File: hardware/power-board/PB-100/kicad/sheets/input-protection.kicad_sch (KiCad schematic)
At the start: 6 parts, among them J1 INPUT_CONNECTOR_CLASS_PRELIM, Q1 INPUT_NMOS_TOLL_PRELIM, U1 LM74700QDBVRQ1_PRELIM, U2 INA228_Q1_PRELIM

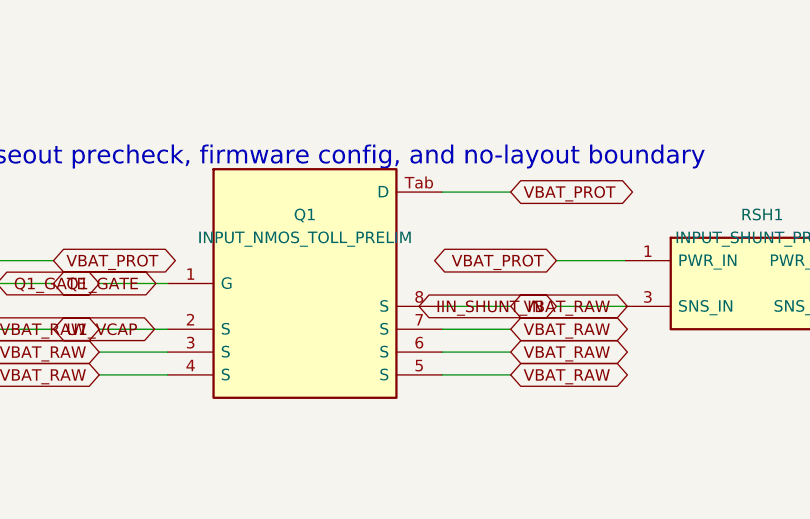
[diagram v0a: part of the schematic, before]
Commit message: feat(hardware): accept CAN1 and 80V freeze decisions
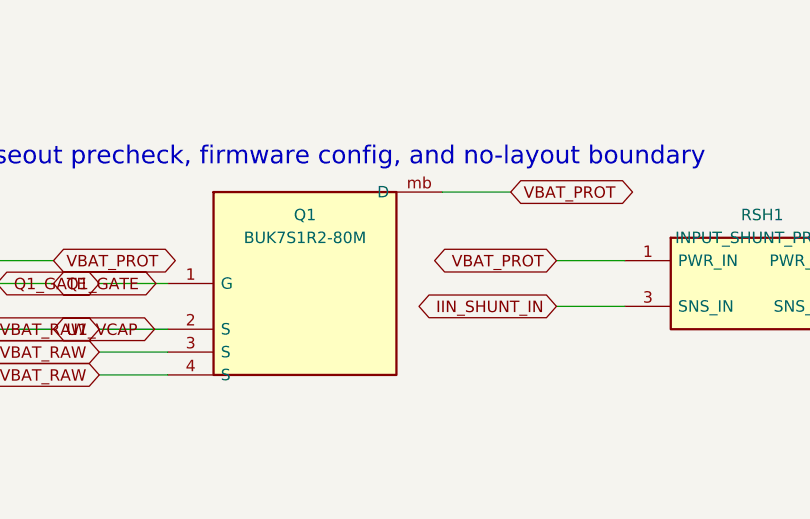
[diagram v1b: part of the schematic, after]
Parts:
- Q1: value INPUT_NMOS_TOLL_PRELIM -> BUK7S1R2-80M; footprint (none) -> PB100:LFPAK88_SOT1235_Nexperia; symbol PB100:PB100_INPUT_NMOS_TOLL_PRELIM -> PB100:PB100_POWER_NMOS_ESCAPE_PRELIM
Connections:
- net VBAT_PROT: now also Q1.mb (D); no longer Q1.Tab (D)
- net VBAT_RAW: no longer Q1.5 (S), Q1.6 (S), Q1.7 (S), Q1.8 (S)
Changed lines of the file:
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@@
   (global_label "VBAT_RAW" (shape bidirectional) (at 129.54 55.88 0) (fields_autoplaced) (effects (font (size 1.27 1.27)) (justify right)) (property "Intersheetrefs" "${INTERSHEET_REFS}" (at 129.54 55.88 0) (effects (font (size 1.27 1.27)) hide)))
   (symbol
-    (lib_id "PB100:PB100_INPUT_NMOS_TOLL_PRELIM")
+    (lib_id "PB100:PB100_POWER_NMOS_ESCAPE_PRELIM")
     (at 203.20 60.96 0)
     (unit 1)
@@
     (dnp no)
     (property "Reference" "Q1" (at 203.20 53.34 0) (effects (font (size 1.27 1.27))))
-    (property "Value" "INPUT_NMOS_TOLL_PRELIM" (at 203.20 55.88 0) (effects (font (size 1.27 1.27))))
-    (property "Footprint" "" (at 203.20 68.58 0) (effects (font (size 1.27 1.27)) hide))
-    (property "Datasheet" "../PB-100-schematic-capture-plan.md" (at 203.20 71.12 0) (effects (font (size 1.27 1.27)) hide))
+    (property "Value" "BUK7S1R2-80M" (at 203.20 55.88 0) (effects (font (size 1.27 1.27))))
+    (property "Footprint" "PB100:LFPAK88_SOT1235_Nexperia" (at 203.20 68.58 0) (effects (font (size 1.27 1.27)) hide))
+    (property "Datasheet" "https://assets.nexperia.com/documents/data-sheet/BUK7S1R2-80M.pdf" (at 203.20 71.12 0) (effects (font (size 1.27 1.27)) hide))
     (pin "1")
     (pin "2")
     (pin "3")
     (pin "4")
-    (pin "5")
-    (pin "6")
-    (pin "7")
-    (pin "8")
-    (pin "Tab")
+    (pin "mb")
     (instances
       (project "PB-100"
@@
   (wire (pts (xy 187.96 71.12) (xy 180.34 71.12)) (stroke (width 0) (type default)))
   (global_label "VBAT_RAW" (shape bidirectional) (at 180.34 71.12 0) (fields_autoplaced) (effects (font (size 1.27 1.27)) (justify right)) (property "Intersheetrefs" "${INTERSHEET_REFS}" (at 180.34 71.12 0) (effects (font (size 1.27 1.27)) hide)))
-  (wire (pts (xy 218.44 71.12) (xy 226.06 71.12)) (stroke (width 0) (type default)))
-  (global_label "VBAT_RAW" (shape bidirectional) (at 226.06 71.12 0) (fields_autoplaced) (effects (font (size 1.27 1.27)) (justify left)) (property "Intersheetrefs" "${INTERSHEET_REFS}" (at 226.06 71.12 0) (effects (font (size 1.27 1.27)) hide)))
-  (wire (pts (xy 218.44 68.58) (xy 226.06 68.58)) (stroke (width 0) (type default)))
-  (global_label "VBAT_RAW" (shape bidirectional) (at 226.06 68.58 0) (fields_autoplaced) (effects (font (size 1.27 1.27)) (justify left)) (property "Intersheetrefs" "${INTERSHEET_REFS}" (at 226.06 68.58 0) (effects (font (size 1.27 1.27)) hide)))
-  (wire (pts (xy 218.44 66.04) (xy 226.06 66.04)) (stroke (width 0) (type default)))
-  (global_label "VBAT_RAW" (shape bidirectional) (at 226.06 66.04 0) (fields_autoplaced) (effects (font (size 1.27 1.27)) (justify left)) (property "Intersheetrefs" "${INTERSHEET_REFS}" (at 226.06 66.04 0) (effects (font (size 1.27 1.27)) hide)))
-  (wire (pts (xy 218.44 63.50) (xy 226.06 63.50)) (stroke (width 0) (type default)))
-  (global_label "VBAT_RAW" (shape bidirectional) (at 226.06 63.50 0) (fields_autoplaced) (effects (font (size 1.27 1.27)) (justify left)) (property "Intersheetrefs" "${INTERSHEET_REFS}" (at 226.06 63.50 0) (effects (font (size 1.27 1.27)) hide)))
   (wire (pts (xy 218.44 50.80) (xy 226.06 50.80)) (stroke (width 0) (type default)))
   (global_label "VBAT_PROT" (shape bidirectional) (at 226.06 50.80 0) (fields_autoplaced) (effects (font (size 1.27 1.27)) (justify left)) (property "Intersheetrefs" "${INTERSHEET_REFS}" (at 226.06 50.80 0) (effects (font (size 1.27 1.27)) hide)))

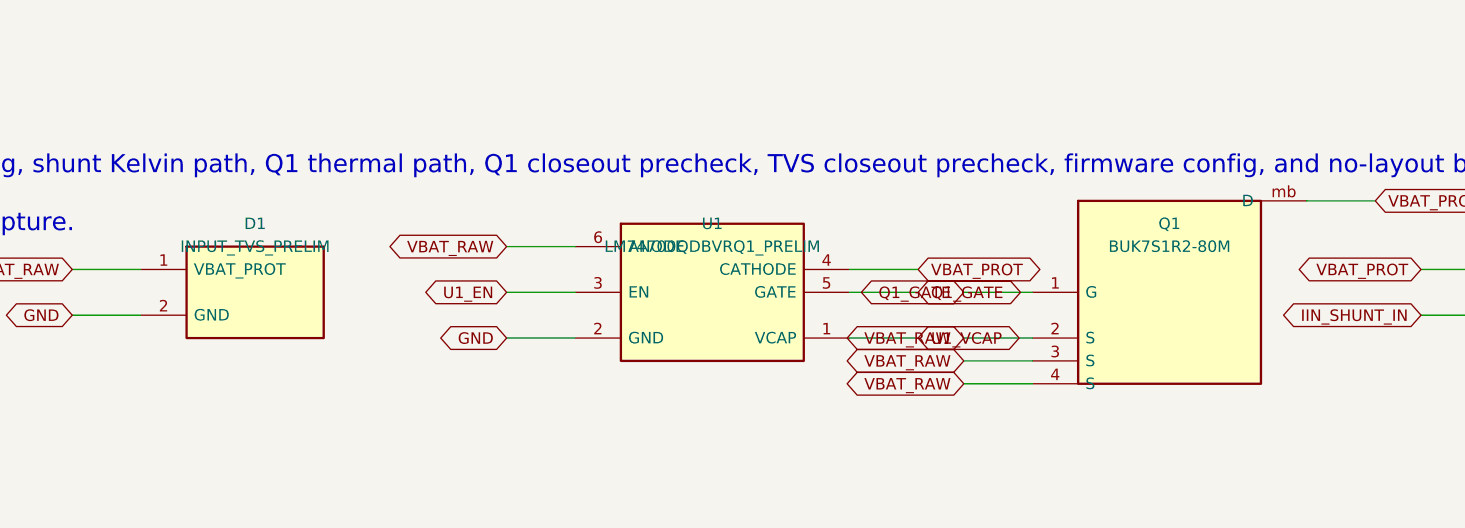
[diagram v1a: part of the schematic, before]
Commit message: feat(pb100): close five pre-layout blockers with generated evidence
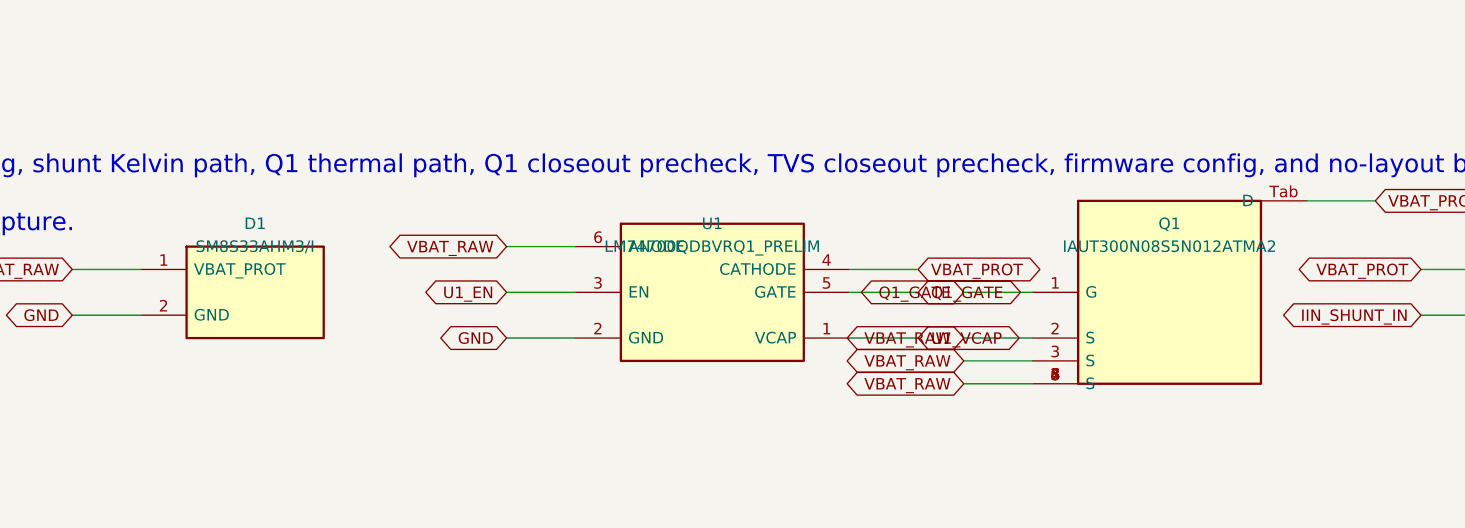
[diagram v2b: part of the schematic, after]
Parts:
- D1: value INPUT_TVS_PRELIM -> SM8S33AHM3/I; footprint (none) -> PB100:DO-218AC_Vishay_SM8S; symbol PB100:PB100_INPUT_TVS_PRELIM -> PB100:PB100_SM8S33AHM3I
- Q1: value BUK7S1R2-80M -> IAUT300N08S5N012ATMA2; footprint PB100:LFPAK88_SOT1235_Nexperia -> PB100:PG-HSOF-8-1_TOLL_Infineon; symbol PB100:PB100_POWER_NMOS_ESCAPE_PRELIM -> PB100:PB100_POWER_NMOS_TOLL_80V
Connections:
- net VBAT_PROT: now also Q1.Tab (D); no longer Q1.mb (D)
- net VBAT_RAW: now also Q1.5 (S), Q1.6 (S), Q1.7 (S), Q1.8 (S)
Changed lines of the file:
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@@
   (global_label "GND_IN" (shape bidirectional) (at 27.94 63.50 0) (fields_autoplaced) (effects (font (size 1.27 1.27)) (justify right)) (property "Intersheetrefs" "${INTERSHEET_REFS}" (at 27.94 63.50 0) (effects (font (size 1.27 1.27)) hide)))
   (symbol
-    (lib_id "PB100:PB100_INPUT_TVS_PRELIM")
+    (lib_id "PB100:PB100_SM8S33AHM3I")
     (at 101.60 60.96 0)
     (unit 1)
@@
     (dnp no)
     (property "Reference" "D1" (at 101.60 53.34 0) (effects (font (size 1.27 1.27))))
-    (property "Value" "INPUT_TVS_PRELIM" (at 101.60 55.88 0) (effects (font (size 1.27 1.27))))
-    (property "Footprint" "" (at 101.60 68.58 0) (effects (font (size 1.27 1.27)) hide))
-    (property "Datasheet" "../PB-100-schematic-capture-plan.md" (at 101.60 71.12 0) (effects (font (size 1.27 1.27)) hide))
+    (property "Value" "SM8S33AHM3/I" (at 101.60 55.88 0) (effects (font (size 1.27 1.27))))
+    (property "Footprint" "PB100:DO-218AC_Vishay_SM8S" (at 101.60 68.58 0) (effects (font (size 1.27 1.27)) hide))
+    (property "Datasheet" "https://www.vishay.com/docs/88392/sm8s.pdf" (at 101.60 71.12 0) (effects (font (size 1.27 1.27)) hide))
     (pin "1")
     (pin "2")
@@
   (global_label "VBAT_RAW" (shape bidirectional) (at 129.54 55.88 0) (fields_autoplaced) (effects (font (size 1.27 1.27)) (justify right)) (property "Intersheetrefs" "${INTERSHEET_REFS}" (at 129.54 55.88 0) (effects (font (size 1.27 1.27)) hide)))
   (symbol
-    (lib_id "PB100:PB100_POWER_NMOS_ESCAPE_PRELIM")
+    (lib_id "PB100:PB100_POWER_NMOS_TOLL_80V")
     (at 203.20 60.96 0)
     (unit 1)
@@
     (dnp no)
     (property "Reference" "Q1" (at 203.20 53.34 0) (effects (font (size 1.27 1.27))))
-    (property "Value" "BUK7S1R2-80M" (at 203.20 55.88 0) (effects (font (size 1.27 1.27))))
-    (property "Footprint" "PB100:LFPAK88_SOT1235_Nexperia" (at 203.20 68.58 0) (effects (font (size 1.27 1.27)) hide))
-    (property "Datasheet" "https://assets.nexperia.com/documents/data-sheet/BUK7S1R2-80M.pdf" (at 203.20 71.12 0) (effects (font (size 1.27 1.27)) hide))
+    (property "Value" "IAUT300N08S5N012ATMA2" (at 203.20 55.88 0) (effects (font (size 1.27 1.27))))
+    (property "Footprint" "PB100:PG-HSOF-8-1_TOLL_Infineon" (at 203.20 68.58 0) (effects (font (size 1.27 1.27)) hide))
+    (property "Datasheet" "https://www.infineon.com/assets/row/public/documents/10/49/infineon-iaut300n08s5n012-datasheet-en.pdf" (at 203.20 71.12 0) (effects (font (size 1.27 1.27)) hide))
     (pin "1")
     (pin "2")
     (pin "3")
     (pin "4")
-    (pin "mb")
+    (pin "5")
+    (pin "6")
+    (pin "7")
+    (pin "8")
+    (pin "Tab")
     (instances
       (project "PB-100"

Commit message: fix(pb100): select active surge cutoff architecture
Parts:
- added CCAP1: 100nF 25V X7R, symbol PB100:PB100_TWO_PIN_COMPONENT
- added CVS1: 100nF 100V X7R, symbol PB100:PB100_TWO_PIN_COMPONENT
- added DZVS1: 56V automotive Zener, symbol PB100:PB100_TWO_PIN_COMPONENT
- added Q2: IAUTN15S6N025ATMA1, PB100:PG-HSOF-8-1_TOLL_Infineon, symbol PB100:PB100_POWER_NMOS_TOLL_150V
- added R3, R4: 42.2k 1%, symbol PB100:PB100_TWO_PIN_COMPONENT
- added R5: 1.00k 1%, symbol PB100:PB100_TWO_PIN_COMPONENT
- added R6: 10k 1%, symbol PB100:PB100_TWO_PIN_COMPONENT
- D1: now not fitted
- U1: value LM74700QDBVRQ1_PRELIM -> LM74930Q1RGERQ1; footprint (none) -> PB100:VQFN-24_RGE_4x4mm_P0.5mm_EP2.4mm; symbol PB100:PB100_LM74700QDBVRQ1_PRELIM -> PB100:PB100_LM74930Q1RGERQ1
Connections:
- net VBAT_PROT_SHUNTED is gone; now on net VBAT_PROT: RSH1.2 (PWR_OUT)
- net GND: now also U1.11 (ILIM), U1.13 (GND), U1.16 (OVCLAMP), U1.9 (TMR), CVS1.2, DZVS1.2, R5.2; no longer U1.2 (GND)
- net VBAT_PROT: no longer Q1.Tab (D), RSH1.1 (PWR_IN), U1.4 (CATHODE)
- net VBAT_RAW: now also Q2.Tab (D), R3.1, R6.1; no longer Q1.2 (S), Q1.3 (S), Q1.4 (S), Q1.5 (S), Q1.6 (S), Q1.7 (S), Q1.8 (S), U1.6 (ANODE)
- net Q1_GATE renamed LM74930_OV
- net LM74930_OV: now also R4.2, R5.1; no longer Q1.1 (G)
- net U1_EN: no longer names the net of U1.3 (SW)
- net U1_VCAP renamed Q1_DGATE
- net Q1_DGATE: now also Q1.1 (G)
- new net INPUT_COMMON_SOURCE: Q1.2 (S), Q1.3 (S), Q1.4 (S), Q1.5 (S), Q1.6 (S), Q1.7 (S), Q1.8 (S), Q2.2 (S), Q2.3 (S), Q2.4 (S), Q2.5 (S), Q2.6 (S), Q2.7 (S), Q2.8 (S), U1.15 (OUT), U1.2 (A)
- new net INPUT_PROT_FAULT_N: U1.12 (FLT)
- new net LM74930_CAP: CCAP1.1, U1.23 (CAP)
- new net LM74930_OV_TOP_MID: R3.2, R4.1
- new net LM74930_VS: CCAP1.2, CVS1.1, DZVS1.1, R6.2, U1.22 (VS), U1.4 (UVLO), U1.6 (EN), U1.7 (MODE)
- new net Q2_HGATE: Q2.1 (G), U1.14 (HGATE)
- new net VBAT_REV_PROT: Q1.Tab (D), RSH1.1 (PWR_IN), U1.18 (ISCP), U1.19 (CS-), U1.20 (CS+), U1.24 (C)
- no-connect marks 0 -> 6
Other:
- note added: "Input protection capture notes: - ADR-0018 selects LM74930-Q1 hard cutoff and permits load disconnection during load dump - Q2 IAUTN15S6N025ATMA1 150 V is the raw-side HGATE cutoff FET - Q1 IAUT300N08S5N012ATMA2 80 V is the protected DGATE reverse FET - R3/R4/R5 42.2k+42.2k/1.00k 1% set a generated 48.99-54.89 V cutoff - D1 SM8S33AHM3/I is DNP legacy footprint only and is not an approved energy s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"
- note removed: "Input protection capture notes: - Source traces: PB-100-input-reverse-package-trace.csv, PB-100-input-reverse-freeze-review.csv, PB-100-input-reverse-q1-freeze-checklist.csv, PB-100-input-reverse-q1-derivation-precheck.csv, PB-100-input-reverse-q1-closeout-precheck.csv, PB-100-board-current-budget-trace.csv, PB-100-board-current-budget-freeze-review.csv, PB-100-board-current-budget-design-calcula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"

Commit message: Fix PBREL-007 Q2 evidence
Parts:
- U1: value LM74930Q1RGERQ1 -> LM74930QRGERQ1; symbol PB100:PB100_LM74930Q1RGERQ1 -> PB100:PB100_LM74930QRGERQ1
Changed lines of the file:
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@@
   (global_label "GND" (shape bidirectional) (at 81.28 63.50 0) (fields_autoplaced) (effects (font (size 1.27 1.27)) (justify right)) (property "Intersheetrefs" "${INTERSHEET_REFS}" (at 81.28 63.50 0) (effects (font (size 1.27 1.27)) hide)))
   (symbol
-    (lib_id "PB100:PB100_LM74930Q1RGERQ1")
+    (lib_id "PB100:PB100_LM74930QRGERQ1")
     (at 152.40 116.84 0)
     (unit 1)
@@
     (dnp no)
     (property "Reference" "U1" (at 152.40 96.52 0) (effects (font (size 1.27 1.27))))
-    (property "Value" "LM74930Q1RGERQ1" (at 152.40 99.06 0) (effects (font (size 1.27 1.27))))
+    (property "Value" "LM74930QRGERQ1" (at 152.40 99.06 0) (effects (font (size 1.27 1.27))))
     (property "Footprint" "PB100:VQFN-24_RGE_4x4mm_P0.5mm_EP2.4mm" (at 152.40 139.70 0) (effects (font (size 1.27 1.27)) hide))
     (property "Datasheet" "https://www.ti.com/lit/ds/symlink/lm74930-q1.pdf" (at 152.40 142.24 0) (effects (font (size 1.27 1.27)) hide))

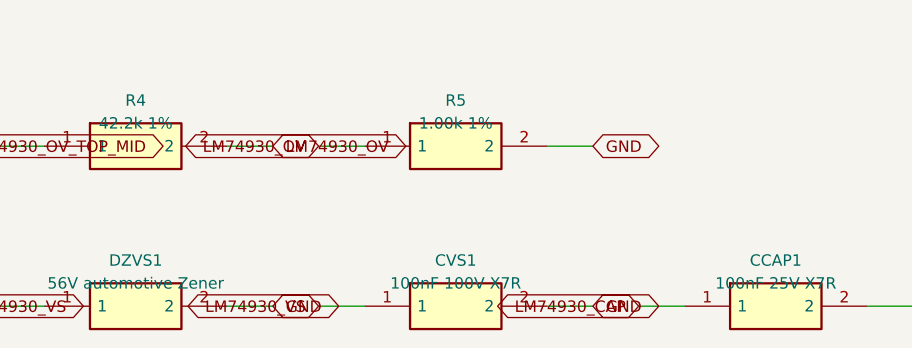
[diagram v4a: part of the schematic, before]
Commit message: feat(pb100): add controlled Q2 qualification coupon
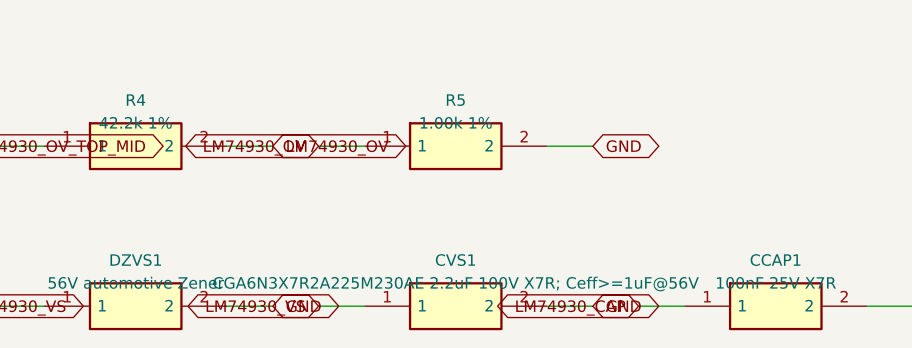
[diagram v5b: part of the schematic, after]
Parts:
- CVS1: value 100nF 100V X7R -> CGA6N3X7R2A225M230AE 2.2uF 100V X7R; Ceff>=1uF@56V
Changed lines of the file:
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@@
     (unit 1) (exclude_from_sim no) (in_bom yes) (on_board yes) (dnp no)
     (property "Reference" "CVS1" (at 147.32 170.18 0) (effects (font (size 1.27 1.27))))
-    (property "Value" "100nF 100V X7R" (at 147.32 172.72 0) (effects (font (size 1.27 1.27))))
+    (property "Value" "CGA6N3X7R2A225M230AE 2.2uF 100V X7R; Ceff>=1uF@56V" (at 147.32 172.72 0) (effects (font (size 1.27 1.27))))
     (property "Footprint" "" (at 147.32 180.34 0) (effects (font (size 1.27 1.27)) hide))
-    (property "Datasheet" "https://www.ti.com/lit/ds/symlink/lm74930-q1.pdf" (at 147.32 182.88 0) (effects (font (size 1.27 1.27)) hide))
+    (property "Datasheet" "https://product.tdk.com/en/search/capacitor/ceramic/mlcc/info?part_no=CGA6N3X7R2A225M230AE" (at 147.32 182.88 0) (effects (font (size 1.27 1.27)) hide))
     (pin "1") (pin "2")
   )
